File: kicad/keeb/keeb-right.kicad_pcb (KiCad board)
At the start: 2 copper layers, 135.4 x 118 mm, 70 parts

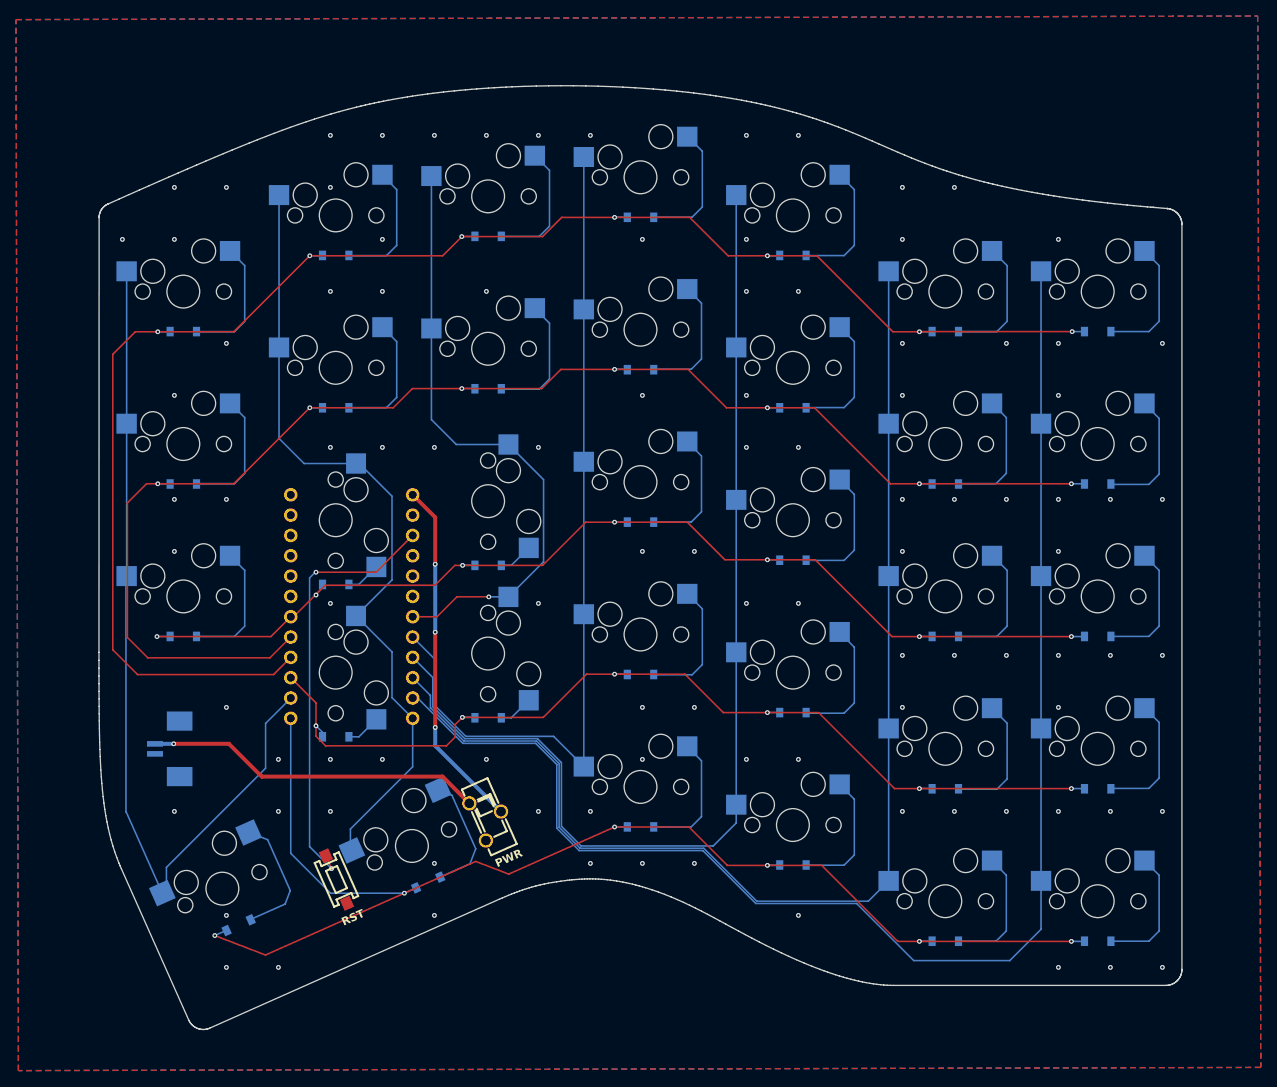
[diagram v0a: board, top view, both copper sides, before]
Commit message: Adding datasheets for switches and connector, updating readme with notes, fixing missing via stitch group on left board
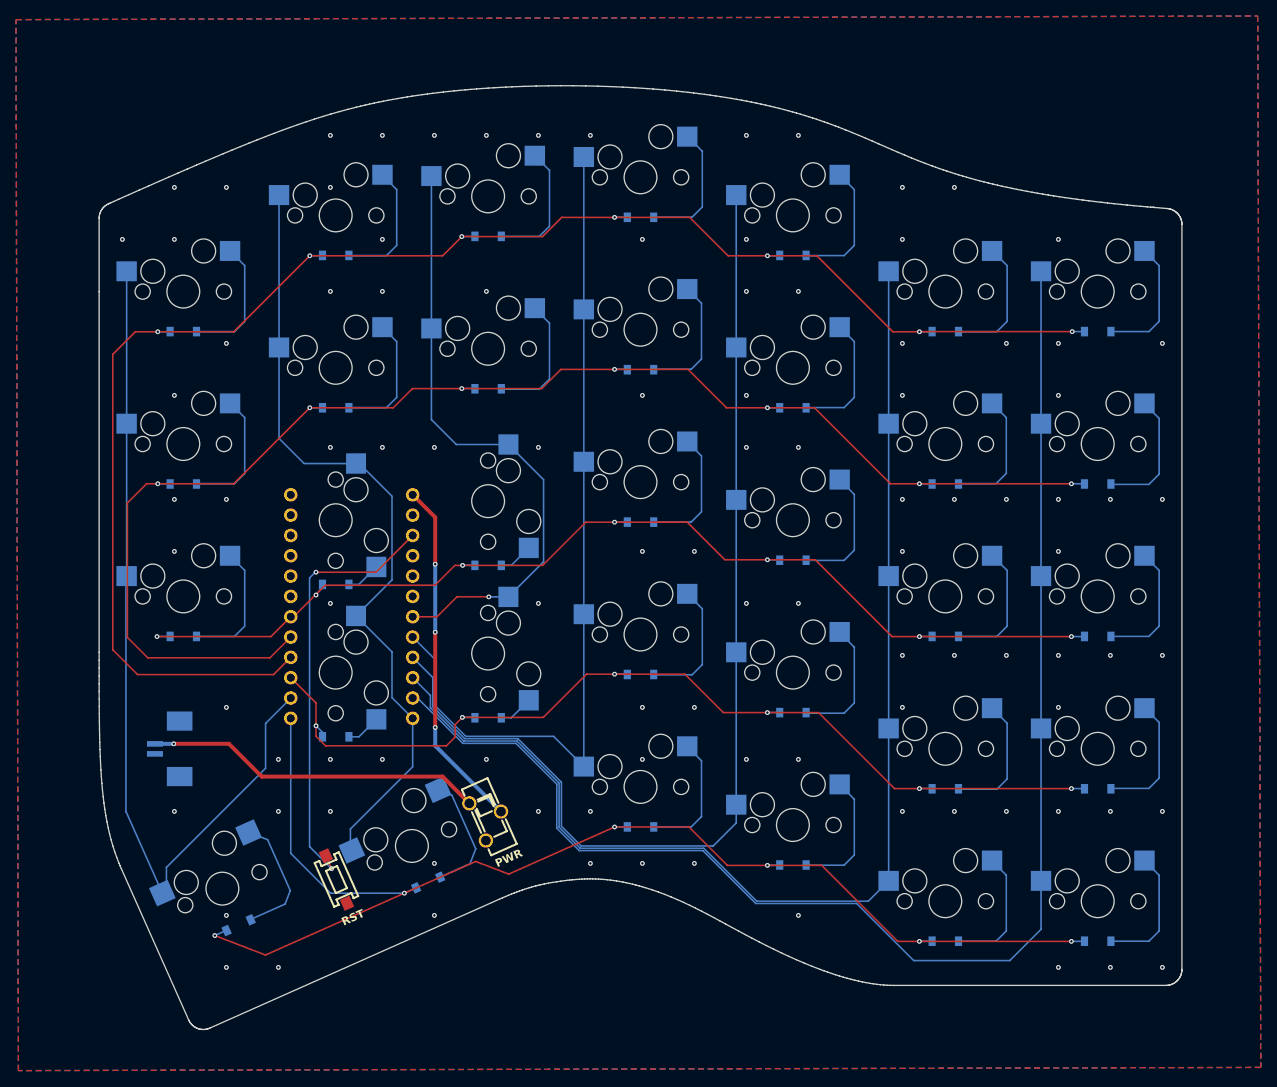
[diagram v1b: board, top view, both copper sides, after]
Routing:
- net P16: track 180.7 -> 179.2 mm
- net P15: track 136.7 -> 135.2 mm
- net P14: track 153.9 -> 152.4 mm
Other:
- outline, holes or cut-outs redrawn
